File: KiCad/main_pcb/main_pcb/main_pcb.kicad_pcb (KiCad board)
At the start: 2 copper layers, 92.3 x 80.5 mm, 49 parts, among them J1 Conn_01x06, J2 Conn_01x21, J3 Conn_01x13, J4 Conn_01x07, J5 Conn_01x07, J6 USB_C_Receptacle_USB2.0_14P, J7 Conn_01x01, J8 Conn_01x01, SW1 SW_Push, U1 ATmega2560-16A, U2 TXB0104D, U3 TXB0104D, U4 TXB0104D, U5 CH340C, U6 AMS1117-3.3, Y1 Crystal_GND24

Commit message: feat(pcb): Second draft
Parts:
- moved SW1 154.9 mm to (68.4, 99.7), turned to -90 degrees
- moved C2 124.6 mm to (88.8, 119.6), turned to -90 degrees
- moved R7 121.7 mm to (118.1, 110.5), turned to 180 degrees
- moved J6 120.9 mm to (125.1, 107.3)
- moved R8 119.5 mm to (118.1, 105.7)
- moved C17 117.4 mm to (105.9, 112.7), turned to 180 degrees
- moved C18 117.3 mm to (116.9, 108.8), turned to 0 degrees
- moved C13 117.2 mm to (82.0, 64.0), turned to 0 degrees
- moved C19 116.7 mm to (105.9, 108.9)
- moved U5 116.7 mm to (111.4, 108.2)
- moved J5 115.6 mm to (83.2, 66.6), turned to -90 degrees
- moved J8 115.6 mm to (117.9, 103.0)
- moved U1 110.2 mm to (89.7, 109.2)
- moved R1 110.0 mm to (80.2, 104.9)
- moved C1 109.9 mm to (99.2, 104.5), turned to -90 degrees
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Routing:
- net /USB-C/TXD: track 107.3 -> 26.2 mm, vias 4 -> 2
- net /USB-C/RXD: track 105.0 -> 26.3 mm, vias 8 -> 2
- net VCC: track 262.4 -> 187.7 mm, vias 6 -> 0
- net /USB-C/USB-C_RST: track 103.1 -> 53.4 mm, vias 2 -> 4
- net /MISO: track 87.6 -> 38.9 mm
- net 3V3: track 144.3 -> 105.7 mm, vias 2 -> 0
- net /SCK: track 68.7 -> 30.5 mm, vias 4 -> 0
- net /MOSI: track 59.6 -> 31.2 mm, vias 4 -> 0
- net /R3: track 31.6 -> 51.6 mm, vias 2 -> 0
- net /Screens/SCK_3V3: track 61.7 -> 42.0 mm, vias 3 -> 0
- net Net-(J5-Pin_6): track 21.1 -> 36.1 mm, vias 0 -> 2
- net Net-(J3-Pin_4): track 11.8 -> 26.3 mm, vias 1 -> 0
- net /SDA: track 41.6 -> 29.1 mm
- net /SCL: track 42.7 -> 30.7 mm
- net Net-(J3-Pin_3): track 16.4 -> 27.9 mm, vias 3 -> 0
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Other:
- board size 92.3 x 80.5 mm -> 69.7 x 75.1 mm

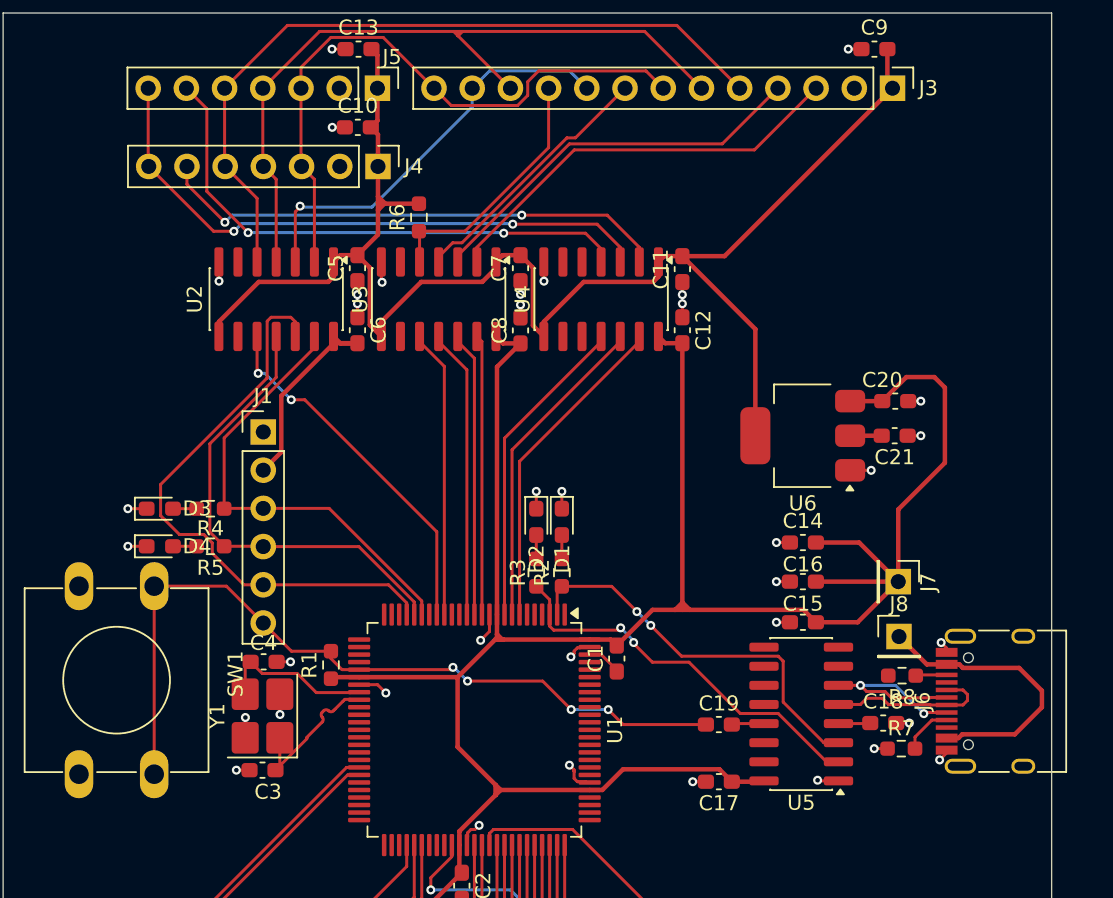
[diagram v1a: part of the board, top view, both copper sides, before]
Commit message: feat(pdf): Updates schematic PDF
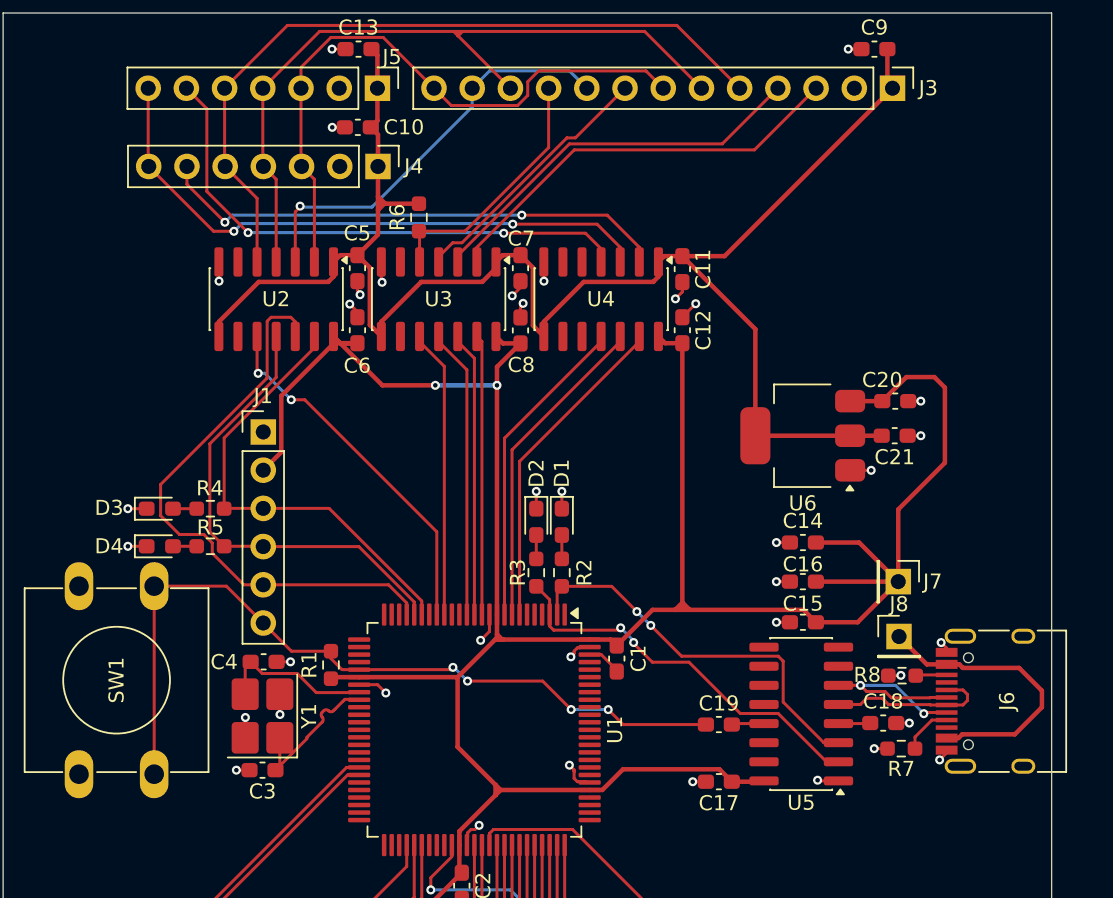
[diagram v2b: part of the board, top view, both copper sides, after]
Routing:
- net VCC: track 187.7 -> 199.9 mm, vias 0 -> 2
- net 3V3: track 105.7 -> 112.0 mm
- net GND: track 43.0 -> 45.5 mm, vias 38 -> 39

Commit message: feat(PCB): Updates PCB layout after Christian's review, thansk a lot Christian :) !
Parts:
- added REF**: MountingHole_3.2mm_M3, MountingHole:MountingHole_3.2mm_M3, F.Cu at (65.0, 78.6)
- added REF**1: MountingHole_3.2mm_M3, MountingHole:MountingHole_3.2mm_M3, F.Cu at (120.0, 78.6)
- added REF**2: MountingHole_3.2mm_M3, MountingHole:MountingHole_3.2mm_M3, F.Cu at (65.0, 118.6)
- added REF**3: MountingHole_3.2mm_M3, MountingHole:MountingHole_3.2mm_M3, F.Cu at (120.0, 118.6)
- C3, C4: value 33pF -> 22pF
- moved C13 10.4 mm to (82.6, 74.4)
- moved C9 5.20 mm to (116.1, 69.2)
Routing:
- net /USB-C/USB-C_RST: track 53.4 -> 40.9 mm
- net 3V3: track 112.0 -> 100.7 mm
- net /USB-C/VBUS: track 19.3 -> 11.8 mm
- net VCC: track 199.9 -> 194.2 mm
- net /R2: track 35.6 -> 33.2 mm
- net GND: track 45.5 -> 47.7 mm
- net /R4: track 30.0 -> 32.1 mm
- net /Screens/SCK_3V3: track 42.0 -> 43.1 mm
- net /R3: track 51.6 -> 52.2 mm

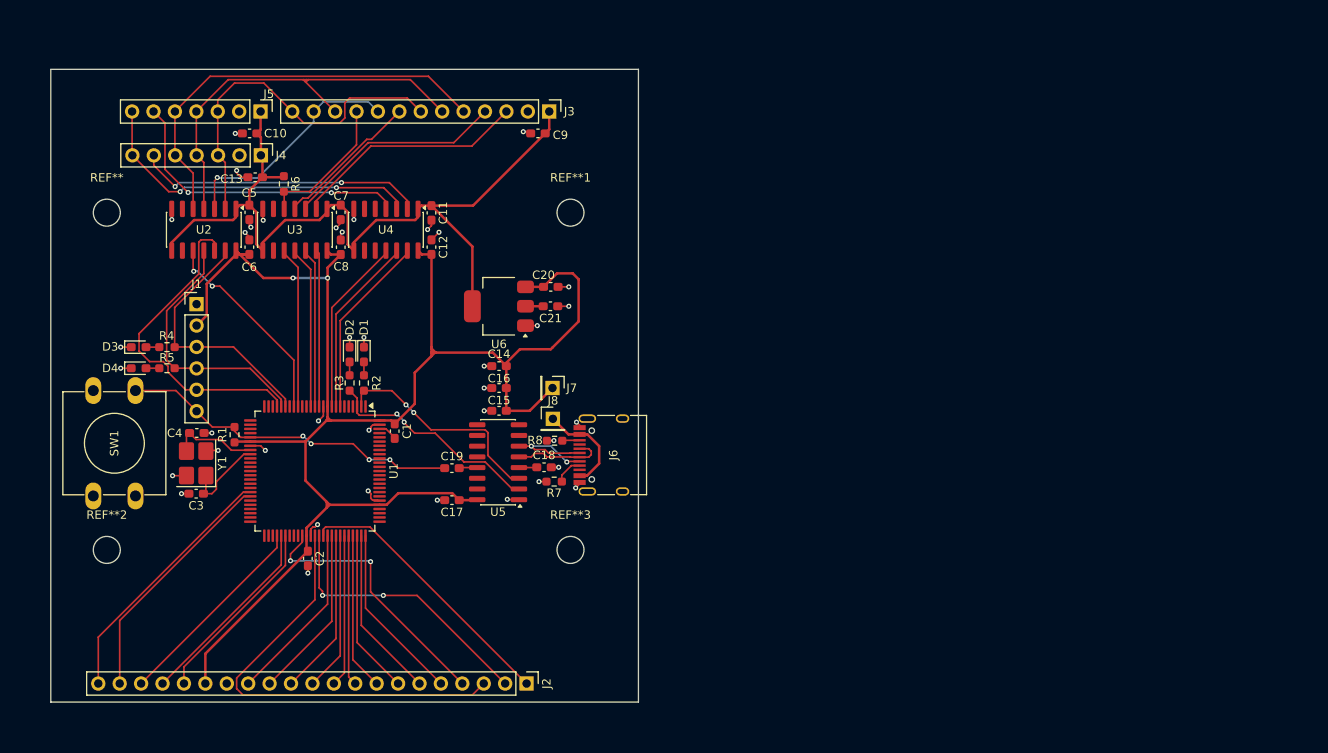
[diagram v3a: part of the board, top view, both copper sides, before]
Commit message: feat(PCB): Adjusts PCB mounting holes.
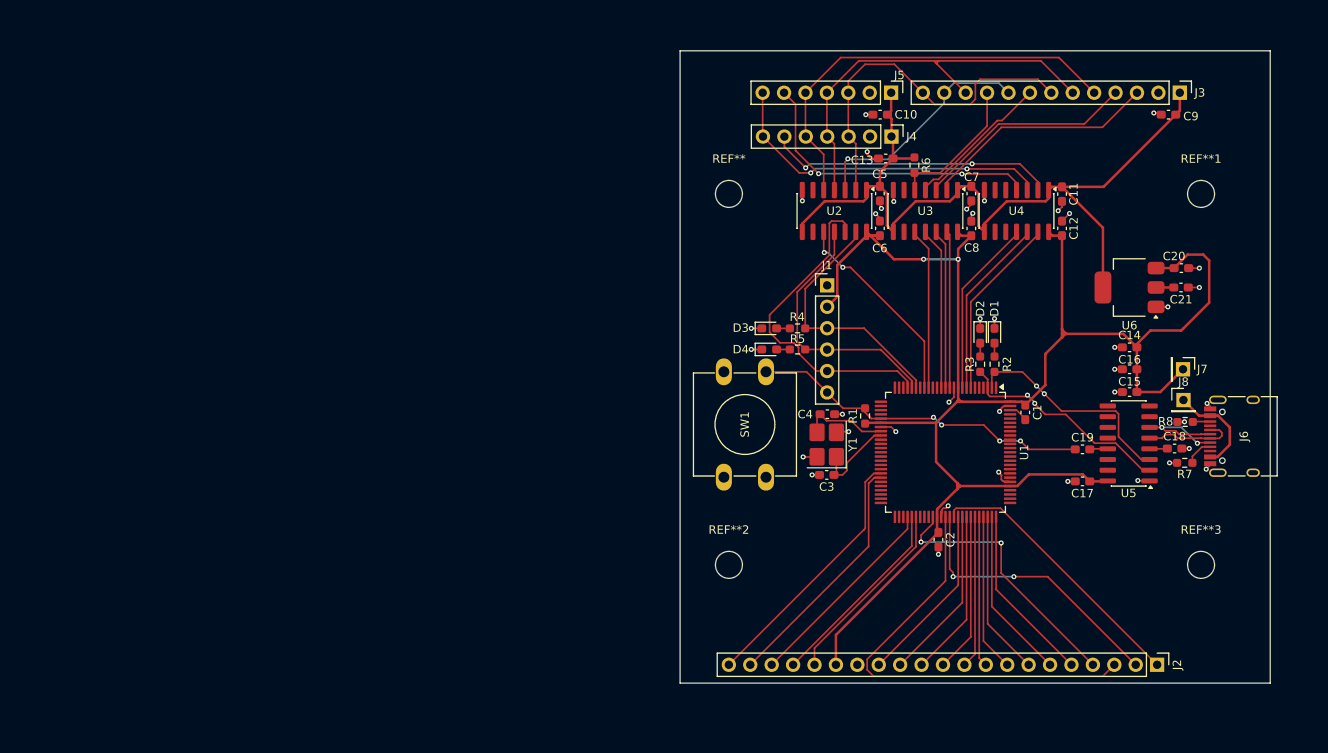
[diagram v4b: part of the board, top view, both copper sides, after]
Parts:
- moved C13 74.8 mm to (157.4, 72.2)
- moved C2 74.8 mm to (163.6, 117.4)
- moved C20 74.8 mm to (192.5, 85.2)
- moved C3 74.8 mm to (150.4, 109.7)
- moved J8 74.8 mm to (192.7, 100.8)
- moved U5 74.8 mm to (186.2, 106.0)
- moved Y1 74.8 mm to (150.4, 106.1)
- moved C11 74.8 mm to (178.3, 76.4)
- moved C12 74.8 mm to (178.3, 80.5)
- moved C18 74.8 mm to (191.7, 106.6)
- moved C4 74.8 mm to (150.5, 102.5)
- moved C9 74.8 mm to (190.9, 67.0)
- moved D2 74.8 mm to (168.6, 93.2)
- moved J2 74.8 mm to (189.6, 132.2)
- moved J3 74.8 mm to (192.3, 64.4)
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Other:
- board size 69.7 x 75.1 mm -> 70 x 75 mm
